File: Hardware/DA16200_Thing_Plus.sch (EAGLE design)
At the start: 63 parts, among them J2 THING_PLUS, J3 Qwiic, J5 USB C, J6 microSD, J7 CORTEX_JTAG_DEBUG_PTH_NS, Q1 20V/4.2A/52mΩ/1.4W, U1 DA16200MOD, U2 CH340E_MSOP10, U3 MCP73831, U5 4MB Flash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

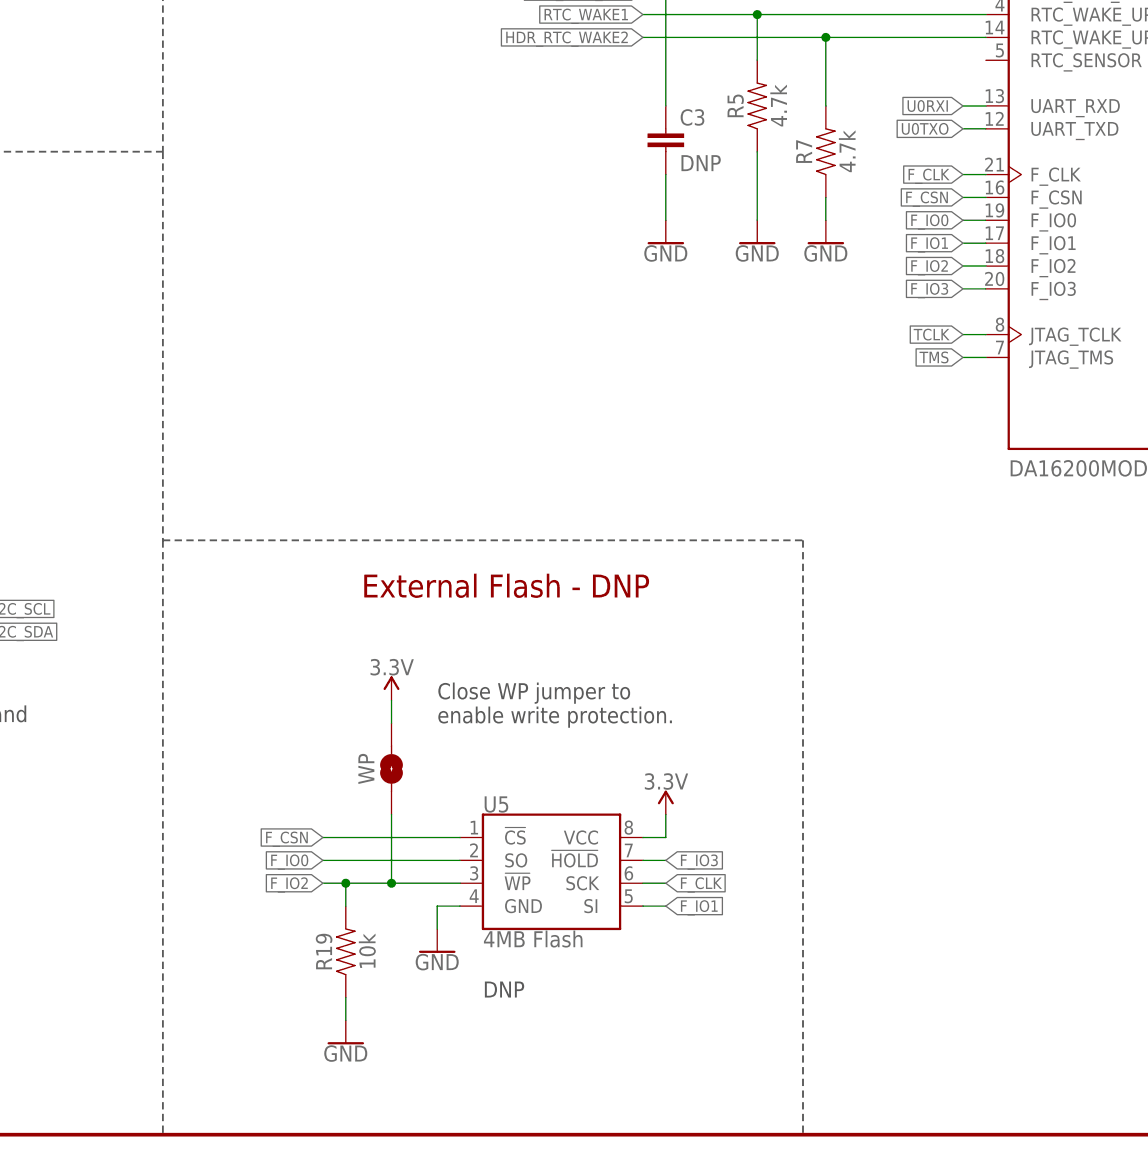
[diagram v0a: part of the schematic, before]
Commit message: Remove external flash!
The "F" pins are the pins internally connecting the DA16200 with the in-module 4MB SFLASH!
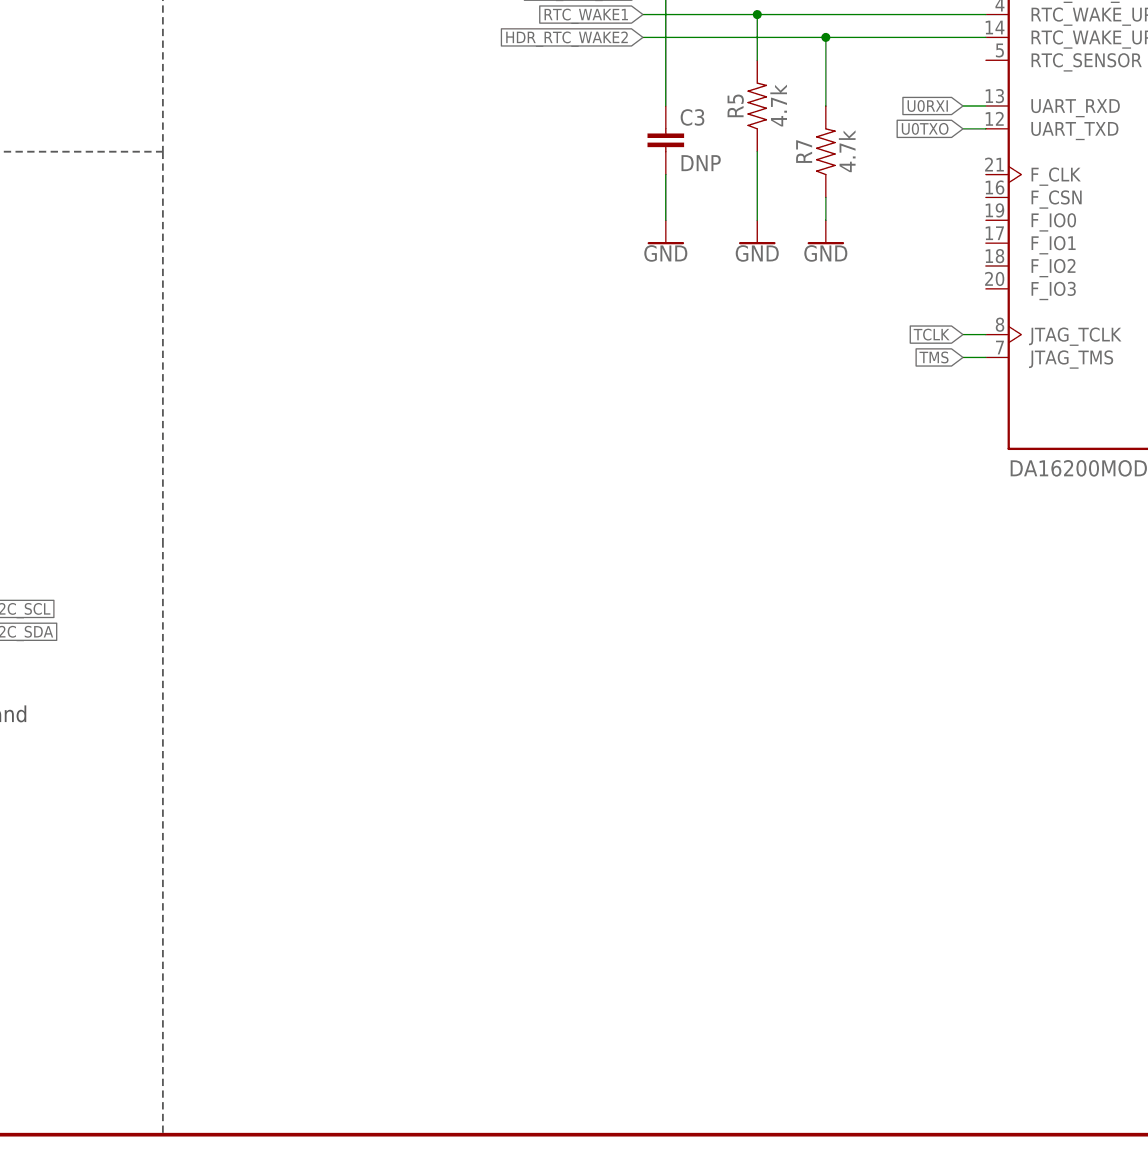
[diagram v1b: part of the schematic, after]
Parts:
- removed R19: 10k, SparkFun-Resistors:10KOHM-0402-1/16W-1%
- removed U5: 4MB Flash, SparkFun-IC-Memory:AT25SF041
- removed WP: JUMPER-SMT_2_NO_SILK, SparkFun-Jumpers:JUMPER-SMT_2_NO_SILK
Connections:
- removed net F_CLK: U1.F_CLK, U5.SCK
- removed net F_CSN: U1.F_CSN, U5.!CS
- removed net F_IO0: U1.F_IO0, U5.SO
- removed net F_IO1: U1.F_IO1, U5.SI
- removed net F_IO2: R19.2, U1.F_IO2, U5.!WP, WP.1
- removed net F_IO3: U1.F_IO3, U5.!HOLD
- net 3.3V: no longer U5.VCC, WP.2
- net GND: no longer R19.1, U5.GND
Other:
- note removed: "Close WP jumper to enable write protection."
- note removed: "DNP"
- note removed: "External Flash - DNP"
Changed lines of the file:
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@@
 <part name="GND23" library="SparkFun-PowerSymbols" deviceset="GND" device=""/>
 <part name="GND24" library="SparkFun-PowerSymbols" deviceset="GND" device=""/>
-<part name="U5" library="SparkFun-IC-Memory" deviceset="AT25SF041" device="" value="4MB Flash"/>
-<part name="GND25" library="SparkFun-PowerSymbols" deviceset="GND" device=""/>
-<part name="SUPPLY16" library="SparkFun-PowerSymbols" deviceset="3.3V" device=""/>
-<part name="R19" library="SparkFun-Resistors" deviceset="10KOHM" device="-0402-1/16W-1%" value="10k"/>
-<part name="WP" library="SparkFun-Jumpers" deviceset="JUMPER-SMT_2_NO" device="_SILK" package3d_urn="urn:adsk.eagle:package:39279/1"/>
-<part name="SUPPLY17" library="SparkFun-PowerSymbols" deviceset="3.3V" device=""/>
-<part name="GND26" library="SparkFun-PowerSymbols" deviceset="GND" device=""/>
 <part name="MEAS" library="SparkFun-Jumpers" deviceset="JUMPER-COMBO_2_NC_TRACE" device=""/>
 <part name="LOGO1" library="SparkFun-Aesthetics" deviceset="OSHW-LOGO" device="S"/>
@@
 <wire x1="0" y1="109.22" x2="76.2" y2="109.22" width="0.2032" layer="97" style="longdash"/>
 <text x="172.974" y="180.086" size="2.54" layer="94" font="vector" align="center">DA16200 Module</text>
-<text x="106.68" y="45.72" size="1.778" layer="97" font="vector">Close WP jumper to
-enable write protection.</text>
 <text x="58.42" y="256.54" size="1.778" layer="97" font="vector">Cut MEAS jumper to measure
 input current from either USB or
 LiPo battery.</text>
-<wire x1="76.2" y1="66.04" x2="147.32" y2="66.04" width="0.2032" layer="97" style="longdash"/>
-<wire x1="147.32" y1="66.04" x2="147.32" y2="0" width="0.2032" layer="97" style="longdash"/>
-<text x="114.3" y="60.96" size="2.54" layer="94" font="vector" align="center">External Flash - DNP</text>
 <text x="223.52" y="223.52" size="2.032" layer="97" font="vector" rot="MR0" align="top-right">Cut and resolder
 CHG jumper to
@@
 to remove LED
 from power.</text>
-<text x="111.76" y="15.24" size="1.778" layer="97" font="vector">DNP</text>
 <text x="81.28" y="144.78" size="1.778" layer="97" font="vector">The RTC_PWR_KEY pin enables the
 RTC block. Keep this pin connected
@@
 <attribute name="VALUE" x="317.5" y="213.106" size="1.778" layer="96" align="top-center"/>
 </instance>
-<instance part="U5" gate="G$1" x="119.38" y="27.94" smashed="yes">
-<attribute name="NAME" x="111.76" y="35.814" size="1.778" layer="95" font="vector"/>
-<attribute name="VALUE" x="111.76" y="22.606" size="1.778" layer="96" font="vector" align="top-left"/>
-</instance>
-<instance part="GND25" gate="1" x="106.68" y="20.32" smashed="yes">
-<attribute name="VALUE" x="106.68" y="20.066" size="1.778" layer="96" align="top-center"/>
-</instance>
-<instance part="SUPPLY16" gate="G$1" x="132.08" y="35.56" smashed="yes">
-<attribute name="VALUE" x="132.08" y="38.354" size="1.778" layer="96" align="bottom-center"/>
-</instance>
-<instance part="R19" gate="G$1" x="96.52" y="20.32" smashed="yes" rot="R90">
-<attribute name="NAME" x="94.996" y="20.32" size="1.778" layer="95" font="vector" rot="R90" align="bottom-center"/>
-<attribute name="VALUE" x="98.044" y="20.32" size="1.778" layer="96" font="vector" rot="R90" align="top-center"/>
-</instance>
-<instance part="WP" gate="G$1" x="101.6" y="40.64" smashed="yes" rot="R90">
-<attribute name="NAME" x="98.806" y="40.64" size="1.778" layer="95" font="vector" rot="R90" align="center"/>
-</instance>
-<instance part="SUPPLY17" gate="G$1" x="101.6" y="48.26" smashed="yes">
-<attribute name="VALUE" x="101.6" y="51.054" size="1.778" layer="96" align="bottom-center"/>
-</instance>
-<instance part="GND26" gate="1" x="96.52" y="10.16" smashed="yes">
-<attribute name="VALUE" x="96.52" y="9.906" size="1.778" layer="96" align="top-center"/>
-</instance>
 <instance part="MEAS" gate="JP1" x="55.88" y="236.22" smashed="yes">
 <attribute name="NAME" x="55.88" y="239.014" size="1.778" layer="95" font="vector" align="center"/>
@@
 </segment>
 <segment>
-<pinref part="U5" gate="G$1" pin="VCC"/>
-<wire x1="129.54" y1="33.02" x2="132.08" y2="33.02" width="0.1524" layer="91"/>
-<wire x1="132.08" y1="33.02" x2="132.08" y2="35.56" width="0.1524" layer="91"/>
-<pinref part="SUPPLY16" gate="G$1" pin="3.3V"/>
-</segment>
-<segment>
-<pinref part="WP" gate="G$1" pin="2"/>
-<pinref part="SUPPLY17" gate="G$1" pin="3.3V"/>
-<wire x1="101.6" y1="48.26" x2="101.6" y2="45.72" width="0.1524" layer="91"/>
-</segment>
-<segment>
 <pinref part="R21" gate="G$1" pin="2"/>
 <pinref part="SUPPLY18" gate="G$1" pin="3.3V"/>
@@
 <wire x1="317.5" y1="215.9" x2="317.5" y2="218.44" width="0.1524" layer="91"/>
 <pinref part="GND24" gate="1" pin="GND"/>
-</segment>
-<segment>
-<pinref part="U5" gate="G$1" pin="GND"/>
-<wire x1="109.22" y1="25.4" x2="106.68" y2="25.4" width="0.1524" layer="91"/>
-<wire x1="106.68" y1="25.4" x2="106.68" y2="22.86" width="0.1524" layer="91"/>
-<pinref part="GND25" gate="1" pin="GND"/>
-</segment>
-<segment>
-<pinref part="R19" gate="G$1" pin="1"/>
-<pinref part="GND26" gate="1" pin="GND"/>
-<wire x1="96.52" y1="12.7" x2="96.52" y2="15.24" width="0.1524" layer="91"/>
 </segment>
 </net>
@@
 </segment>
 </net>
-<net name="F_CLK" class="0">
-<segment>
-<pinref part="U1" gate="G$1" pin="F_CLK"/>
-<wire x1="167.64" y1="106.68" x2="165.1" y2="106.68" width="0.1524" layer="91"/>
-<label x="165.1" y="106.68" size="1.27" layer="95" rot="R180" xref="yes"/>
-</segment>
-<segment>
-<pinref part="U5" gate="G$1" pin="SCK"/>
-<wire x1="129.54" y1="27.94" x2="132.08" y2="27.94" width="0.1524" layer="91"/>
-<label x="132.08" y="27.94" size="1.27" layer="95" xref="yes"/>
-</segment>
-</net>
-<net name="F_CSN" class="0">
-<segment>
-<pinref part="U1" gate="G$1" pin="F_CSN"/>
-<wire x1="167.64" y1="104.14" x2="165.1" y2="104.14" width="0.1524" layer="91"/>
-<label x="165.1" y="104.14" size="1.27" layer="95" rot="R180" xref="yes"/>
-</segment>
-<segment>
-<pinref part="U5" gate="G$1" pin="!CS"/>
-<wire x1="109.22" y1="33.02" x2="93.98" y2="33.02" width="0.1524" layer="91"/>
-<label x="93.98" y="33.02" size="1.27" layer="95" rot="R180" xref="yes"/>
-</segment>
-</net>
-<net name="F_IO0" class="0">
-<segment>
-<pinref part="U1" gate="G$1" pin="F_IO0"/>
-<wire x1="167.64" y1="101.6" x2="165.1" y2="101.6" width="0.1524" layer="91"/>
-<label x="165.1" y="101.6" size="1.27" layer="95" rot="R180" xref="yes"/>
-</segment>
-<segment>
-<pinref part="U5" gate="G$1" pin="SO"/>
-<wire x1="109.22" y1="30.48" x2="93.98" y2="30.48" width="0.1524" layer="91"/>
-<label x="93.98" y="30.48" size="1.27" layer="95" rot="R180" xref="yes"/>
-</segment>
-</net>
-<net name="F_IO1" class="0">
-<segment>
-<pinref part="U1" gate="G$1" pin="F_IO1"/>
-<wire x1="167.64" y1="99.06" x2="165.1" y2="99.06" width="0.1524" layer="91"/>
-<label x="165.1" y="99.06" size="1.27" layer="95" rot="R180" xref="yes"/>
-</segment>
-<segment>
-<pinref part="U5" gate="G$1" pin="SI"/>
-<wire x1="129.54" y1="25.4" x2="132.08" y2="25.4" width="0.1524" layer="91"/>
-<label x="132.08" y="25.4" size="1.27" layer="95" xref="yes"/>
-</segment>
-</net>
-<net name="F_IO2" class="0">
-<segment>
-<pinref part="U1" gate="G$1" pin="F_IO2"/>
-<wire x1="167.64" y1="96.52" x2="165.1" y2="96.52" width="0.1524" layer="91"/>
-<label x="165.1" y="96.52" size="1.27" layer="95" rot="R180" xref="yes"/>
-</segment>
-<segment>
-<pinref part="U5" gate="G$1" pin="!WP"/>
-<wire x1="109.22" y1="27.94" x2="101.6" y2="27.94" width="0.1524" layer="91"/>
-<label x="93.98" y="27.94" size="1.27" layer="95" rot="R180" xref="yes"/>
-<pinref part="WP" gate="G$1" pin="1"/>
-<wire x1="101.6" y1="27.94" x2="96.52" y2="27.94" width="0.1524" layer="91"/>
-<wire x1="96.52" y1="27.94" x2="93.98" y2="27.94" width="0.1524" layer="91"/>
-<wire x1="101.6" y1="35.56" x2="101.6" y2="27.94" width="0.1524" layer="91"/>
-<junction x="101.6" y="27.94"/>
-<pinref part="R19" gate="G$1" pin="2"/>
-<wire x1="96.52" y1="27.94" x2="96.52" y2="25.4" width="0.1524" layer="91"/>
-<junction x="96.52" y="27.94"/>
-</segment>
-</net>
-<net name="F_IO3" class="0">
-<segment>
-<pinref part="U1" gate="G$1" pin="F_IO3"/>
-<wire x1="167.64" y1="93.98" x2="165.1" y2="93.98" width="0.1524" layer="91"/>
-<label x="165.1" y="93.98" size="1.27" layer="95" rot="R180" xref="yes"/>
-</segment>
-<segment>
-<pinref part="U5" gate="G$1" pin="!HOLD"/>
-<wire x1="129.54" y1="30.48" x2="132.08" y2="30.48" width="0.1524" layer="91"/>
-<label x="132.08" y="30.48" size="1.27" layer="95" xref="yes"/>
-</segment>
-</net>
